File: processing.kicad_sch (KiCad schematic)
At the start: 47 parts, among them IC10 MT29F2G01ABAGDWB-IT_G_TR, IC2 XMC7200D-E272K8384AA, IC6 DS90LV011AHMF_NOPB, IC9 MT29F2G01ABAGDWB-IT_G_TR, Q1 ZXT849K, Y1 DSC1101DM2-012.0000

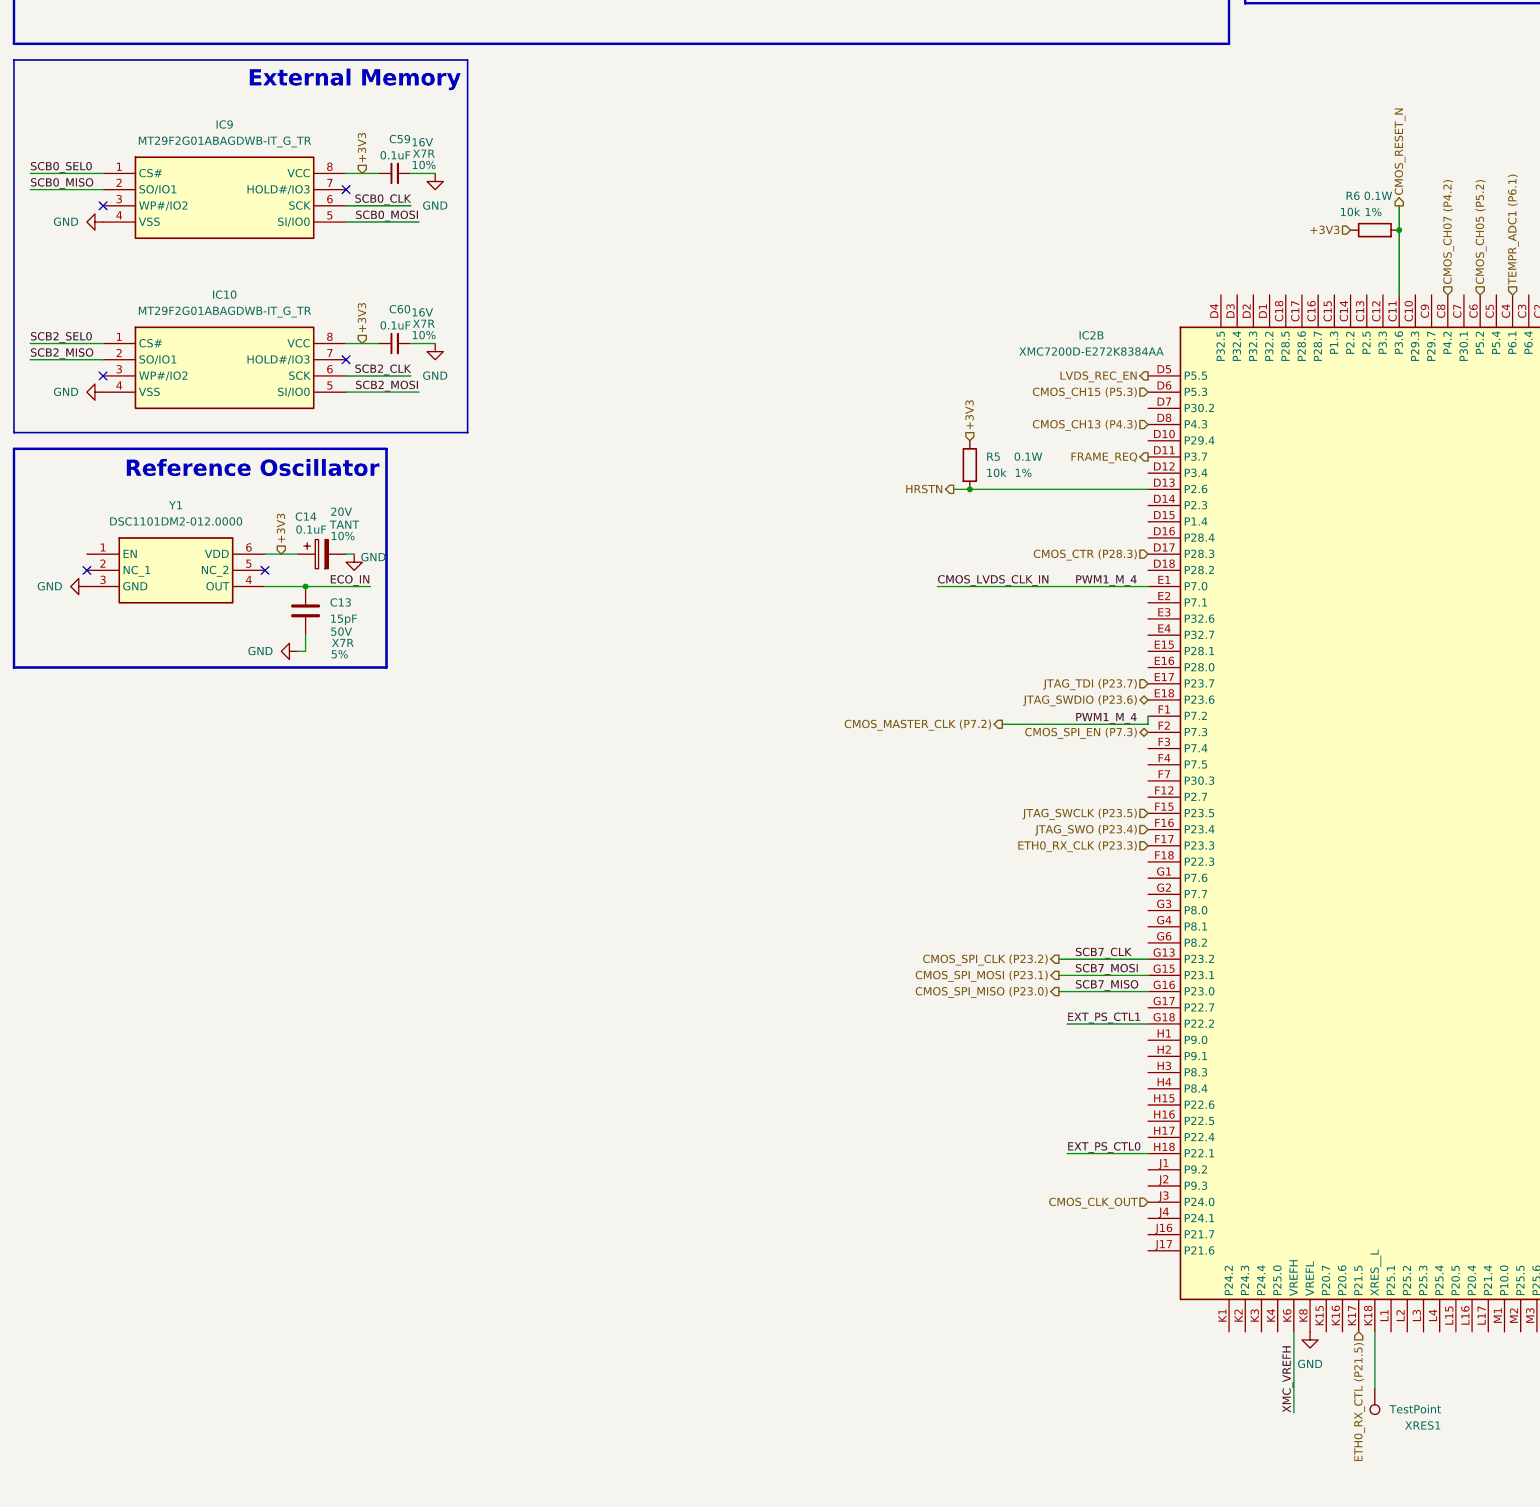
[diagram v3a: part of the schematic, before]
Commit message: QSPI Lines for 100 MHz channel
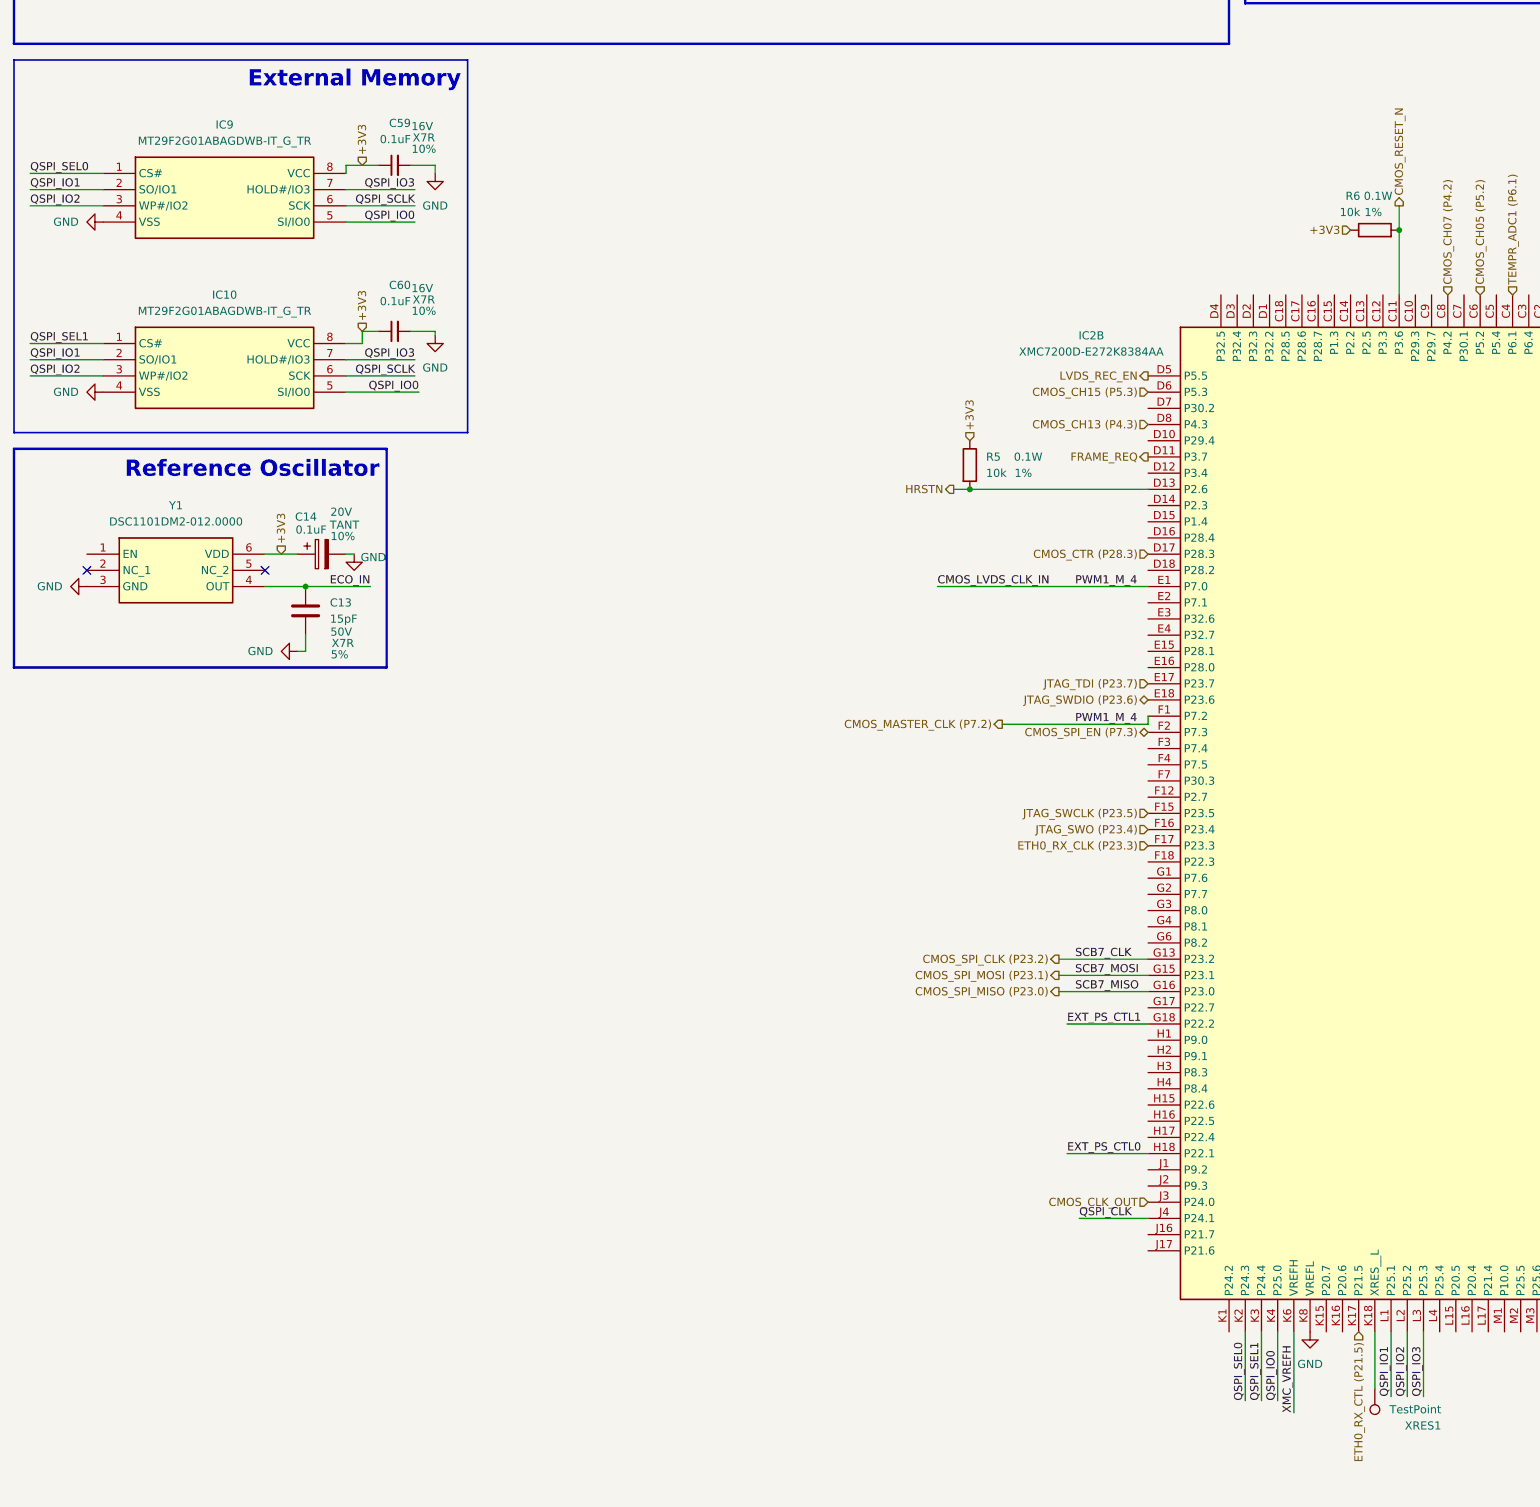
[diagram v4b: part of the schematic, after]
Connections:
- net SCB0_CLK: no longer IC9.6 (SCK)
- net SCB0_MISO: no longer IC9.2 (SO/IO1)
- net SCB0_MOSI: no longer IC9.5 (SI/IO0)
- net SCB0_SEL0: no longer IC9.1 (CS#)
- net SCB2_CLK: no longer IC10.6 (SCK)
- net SCB2_MISO: no longer IC10.2 (SO/IO1)
- net SCB2_MOSI: no longer IC10.5 (SI/IO0)
- net SCB2_SEL0: no longer IC10.1 (CS#)
- net QSPI_IO2: now reaches IC9.3 (WP#/IO2)
- net QSPI_IO2: now also IC10.3 (WP#/IO2), IC2.L2 (P25.2)
- net QSPI_IO3: now reaches IC9.7 (HOLD#/IO3)
- net QSPI_IO3: now also IC10.7 (HOLD#/IO3), IC2.L3 (P25.3)
- net QSPI_CLK: now reaches IC2.J4 (P24.1)
- net QSPI_SEL0: now reaches IC2.K2 (P24.3)
- net QSPI_SEL0: now also IC9.1 (CS#)
- net QSPI_SEL1: now reaches IC2.K3 (P24.4)
- net QSPI_SEL1: now also IC10.1 (CS#)
- net QSPI_IO0: now reaches IC2.K4 (P25.0)
- net QSPI_IO0: now also IC10.5 (SI/IO0), IC9.5 (SI/IO0)
- net QSPI_IO1: now reaches IC2.L1 (P25.1)
- net QSPI_IO1: now also IC10.2 (SO/IO1), IC9.2 (SO/IO1)
- new net QSPI_SCLK: IC10.6 (SCK), IC9.6 (SCK)
- no-connect marks 6 -> 2
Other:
- moved on the sheet: C59, C60

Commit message: Some small changes for BOM
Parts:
- VCORE1, XRES1: now left out of the parts list
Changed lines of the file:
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@@
 		(unit 1)
 		(exclude_from_sim no)
-		(in_bom yes)
+		(in_bom no)
 		(on_board yes)
 		(dnp no)
@@
 		(unit 1)
 		(exclude_from_sim no)
-		(in_bom yes)
+		(in_bom no)
 		(on_board yes)
 		(dnp no)

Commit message: Ethernet Transceiver
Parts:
- renumbered C16 to C29, C71 to C30, C36 to C31, C51 to C32, C15 to C33, C52 to C34, C23 to C35, C62 to C36, C13 to C37, C37 to C38, C14 to C39, C25 to C40, C38 to C41, C59 to C42, C60 to C43, C54 to C44, C39 to C45, C41 to C46, C49 to C47, C43 to C48, C40 to C49, C55 to C50, C42 to C51, C69 to C52, C44 to C53, C45 to C54, C48 to C55, C57 to C56, C58 to C57, C53 to C58, C46 to C59, C61 to C60, C50 to C61, C33 to C62, C11 to C63, C12 to C64, IC9 to IC4, IC10 to IC5, IC2 to IC6, IC6 to IC7, R5 to R4, R6 to R5, R4 to R6

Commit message: Memory layout completed
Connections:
- net QSPI_CLK is gone; now on net QSPI_SCLK: IC6.J4 (P24.1)

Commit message: Lots of PCB changes, some small parts changes
Updated parts footprints from those found in MDE Lab. Some parameters may be incorrect, but all footprints should be correct
Drew most of PCB. CMOS SPI still needs connection. Decoupling caps on MCU still need connection. Power and ground needs to be analyzed, and some components may not have power or ground connected.
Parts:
- C37: footprint (none) -> Capacitor_SMD:C_0603_1608Metric
- R4, R5: footprint Resistor_SMD:R_0603_1608Metric -> Resistor_SMD:R_1206_3216Metric; Power Rating 0.1W -> 0.25W
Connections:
- net +3V3: no longer C47.1, C49.1, C51.1, C53.1, C54.1, C62.1, IC6.F13 (VCCD_2), IC6.F6 (VCCD_1), IC6.G18 (P22.2), IC6.N13 (VCCD_4), IC6.N6 (VCCD_3), R6.2, VCORE1.1
- net CMOS_CH01 (P5.0): now also IC6.A2 (P6.5); no longer IC6.A6 (P5.0)
- net CMOS_CH03 (P4.0): now also IC6.A3 (P6.2); no longer IC6.A8 (P4.0)
- net CMOS_CH05 (P5.2): now also IC6.A4 (P31.2); no longer IC6.C6 (P5.2)
- net CMOS_CH07 (P4.2): now also IC6.A5 (P31.0); no longer IC6.C8 (P4.2)
- net CMOS_CH09 (P4.1): now also IC6.A6 (P5.0); no longer IC6.B8 (P4.1)
- net CMOS_CH11 (P5.1): now also IC6.A7 (P4.4); no longer IC6.B6 (P5.1)
- net CMOS_CH13 (P4.3): now also IC6.A8 (P4.0); no longer IC6.D8 (P4.3)
- net CMOS_CH15 (P5.3): now also IC6.A9 (P29.5); no longer IC6.D6 (P5.3)
- net CMOS_CLK_OUT: now also IC6.C18 (P28.5); no longer IC6.J3 (P24.0)
- net TEMPR_ADC0 (P6.0): now also IC6.U1 (P12.6); no longer IC6.B4 (P6.0)
- net TEMPR_ADC1 (P6.1): now also IC6.V2 (P13.0); no longer IC6.C4 (P6.1)
- net CMOS_CTR_OUT (P28.3): now reaches IC6.C2 (P32.1)
- net CMOS_CTR (P28.3): no longer names the net of IC6.D17 (P28.3)
- new net EXT_PS_CTL1: C47.1, C49.1, C51.1, C53.1, C54.1, C62.1, IC6.F13 (VCCD_2), IC6.F6 (VCCD_1), IC6.G18 (P22.2), IC6.N13 (VCCD_4), IC6.N6 (VCCD_3), R6.2, VCORE1.1
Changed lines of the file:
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@@
 	)
 	(junction
+		(at 137.16 35.56)
+		(diameter 0)
+		(color 0 0 0 0)
+	)
+	(junction
 		(at 21.59 34.29)
 		(diameter 0)
@@
 	(wire
 		(pts
+			(xy 179.07 237.49) (xy 191.77 237.49)
+		)
+		(stroke
+			(width 0)
+			(type default)
+		)
+	)
+	(wire
+		(pts
 			(xy 151.13 68.58) (xy 151.13 67.31)
 		)
@@
 	(wire
 		(pts
-			(xy 179.07 237.49) (xy 191.77 237.49)
-		)
-		(stroke
-			(width 0)
-			(type default)
-		)
-	)
-	(wire
-		(pts
 			(xy 191.77 190.5) (xy 191.77 189.23)
 		)
@@
 	(wire
 		(pts
+			(xy 137.16 24.13) (xy 137.16 35.56)
+		)
+		(stroke
+			(width 0)
+			(type default)
+		)
+	)
+	(wire
+		(pts
 			(xy 106.68 35.56) (xy 106.68 36.83)
 		)
@@
 		)
 	)
-	(label "EXT_PS_CTL1"
-		(at 210.82 49.53 0)
-		(fields_autoplaced yes)
-		(effects
-			(font
-				(size 1.27 1.27)
-			)
-			(justify left bottom)
-		)
-	)
 	(label "QSPI_IO1"
 		(at 16.51 133.35 0)
@@
 		)
 	)
+	(label "EXT_PS_CTL1"
+		(at 210.82 49.53 0)
+		(fields_autoplaced yes)
+		(effects
+			(font
+				(size 1.27 1.27)
+			)
+			(justify left bottom)
+		)
+	)
 	(label "XMC_VREFH"
 		(at 175.26 24.13 270)
@@
 		)
 	)
+	(label "XMC_VCCD"
+		(at 137.16 24.13 270)
+		(fields_autoplaced yes)
+		(effects
+			(font
+				(size 1.27 1.27)
+			)
+			(justify right bottom)
+		)
+	)
 	(label "QSPI_IO1"
 		(at 229.87 295.91 90)
@@
 		)
 	)
-	(label "EXT_PS_CTL1"
-		(at 179.07 237.49 0)
+	(label "XMC_VDDD"
+		(at 363.22 111.76 270)
 		(fields_autoplaced yes)
 		(effects
@@
 				(size 1.27 1.27)
 			)
-			(justify left bottom)
+			(justify right bottom)
 		)
 	)
-	(label "XMC_VDDD"
-		(at 363.22 111.76 270)
+	(label "EXT_PS_CTL1"
+		(at 179.07 237.49 0)
 		(fields_autoplaced yes)
 		(effects
@@
 				(size 1.27 1.27)
 			)
-			(justify right bottom)
+			(justify left bottom)
 		)
 	)
@@
 	(hierarchical_label "CMOS_CH03 (P4.0)"
 		(shape input)
-		(at 327.66 123.19 90)
+		(at 340.36 123.19 90)
 		(fields_autoplaced yes)
 		(effects
@@
 	(hierarchical_label "TEMPR_ADC0 (P6.0)"
 		(shape input)
-		(at 294.64 123.19 90)
+		(at 389.89 189.23 0)
 		(fields_autoplaced yes)
 		(effects
@@
 		)
 	)
-	(hierarchical_label "+3V3"
-		(shape input)
-		(at 137.16 35.56 0)
-		(fields_autoplaced yes)
-		(effects
-			(font
-				(size 1.27 1.27)
-			)
-			(justify left)
-		)
-	)
 	(hierarchical_label "ETH0_REF_CLK (P18.0)"
 		(shape output)
@@
 	(hierarchical_label "TEMPR_ADC1 (P6.1)"
 		(shape input)
-		(at 248.92 123.19 90)
+		(at 389.89 234.95 0)
 		(fields_autoplaced yes)
 		(effects
@@
 	(hierarchical_label "CMOS_CH13 (P4.3)"
 		(shape input)
-		(at 191.77 143.51 180)
+		(at 327.66 123.19 90)
 		(fields_autoplaced yes)
 		(effects
@@
 				(size 1.27 1.27)
 			)
-			(justify right)
+			(justify left)
 		)
 	)
 	(hierarchical_label "CMOS_CLK_OUT"
 		(shape input)
-		(at 191.77 265.43 180)
+		(at 213.36 123.19 90)
 		(fields_autoplaced yes)
 		(effects
@@
 				(size 1.27 1.27)
 			)
-			(justify right)
+			(justify left)
 		)
 	)
@@
 		)
 	)
-	(hierarchical_label "CMOS_CTR (P28.3)"
+	(hierarchical_label "CMOS_CTR_OUT (P28.3)"
 		(shape input)
-		(at 191.77 163.83 180)
+		(at 254 123.19 90)
 		(fields_autoplaced yes)
 		(effects
@@
 				(size 1.27 1.27)
 			)
-			(justify right)
+			(justify left)
 		)
 	)
@@
 	(hierarchical_label "CMOS_CH11 (P5.1)"
 		(shape input)
-		(at 289.56 123.19 90)
+		(at 330.2 123.19 90)
 		(fields_autoplaced yes)
 		(effects
@@
 	(hierarchical_label "CMOS_CH01 (P5.0)"
 		(shape input)
-		(at 332.74 123.19 90)
+		(at 342.9 123.19 90)
 		(fields_autoplaced yes)
 		(effects
@@
 	(hierarchical_label "CMOS_CH09 (P4.1)"
 		(shape input)
-		(at 284.48 123.19 90)
+		(at 332.74 123.19 90)
 		(fields_autoplaced yes)
 		(effects
@@
 	(hierarchical_label "CMOS_CH15 (P5.3)"
 		(shape input)
-		(at 191.77 138.43 180)
+		(at 325.12 123.19 90)
 		(fields_autoplaced yes)
 		(effects
@@
 				(size 1.27 1.27)
 			)
-			(justify right)
+			(justify left)
 		)
 	)
@@
 	(hierarchical_label "CMOS_CH07 (P4.2)"
 		(shape input)
-		(at 238.76 123.19 90)
+		(at 335.28 123.19 90)
 		(fields_autoplaced yes)
 		(effects
@@
 	(hierarchical_label "CMOS_CH05 (P5.2)"
 		(shape input)
-		(at 243.84 123.19 90)
+		(at 337.82 123.19 90)
 		(fields_autoplaced yes)
 		(effects
@@
 			)
 		)
-		(property "Footprint" "Resistor_SMD:R_0603_1608Metric"
+		(property "Footprint" "Resistor_SMD:R_1206_3216Metric"
 			(at 162.052 149.86 90)
 			(effects
@@
 			)
 		)
-		(property "Power Rating" "0.1W"
+		(property "Power Rating" "0.25W"
 			(at 172.974 148.59 0)
 			(effects
@@
 			)
 		)
-		(property "Footprint" ""
+		(property "Footprint" "Capacitor_SMD:C_0603_1608Metric"
 			(at 60.6552 176.53 0)
 			(effects
@@
 			)
 		)
-		(property "Footprint" "Resistor_SMD:R_0603_1608Metric"
+		(property "Footprint" "Resistor_SMD:R_1206_3216Metric"
 			(at 227.33 114.808 90)
 			(effects
@@
 			)
 		)
-		(property "Power Rating" "0.1W"
+		(property "Power Rating" "0.25W"
 			(at 227.838 107.696 90)
 			(effects
